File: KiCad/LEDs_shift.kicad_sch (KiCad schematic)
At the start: 37 parts, among them J101 2mm_clamp, J102 2mm_clamp, J103 2mm_clamp, J104 2mm_clamp, J105 2mm_clamp, J106 2mm_clamp, J107 2mm_clamp, J108 2mm_clamp, J109 2mm_clamp, J110 2mm_clamp, J111 2mm_clamp, J112 2mm_clamp, J113 2mm_clamp, J114 2mm_clamp, J115 2mm_clamp, J116 2mm_clamp, J117 2mm_clamp, J118 2mm_clamp, J119 2mm_clamp, J120 2mm_clamp, J121 2mm_clamp, J122 2mm_clamp, J123 2mm_clamp, J124 2mm_clamp, J125 2mm_clamp, J126 2mm_clamp, J127 2mm_clamp, J128 2mm_clamp, J129 2mm_clamp, U136 74HC595D,118, U137 74HC595D,118, U138 74HC595D,118, U139 74HC595D,118

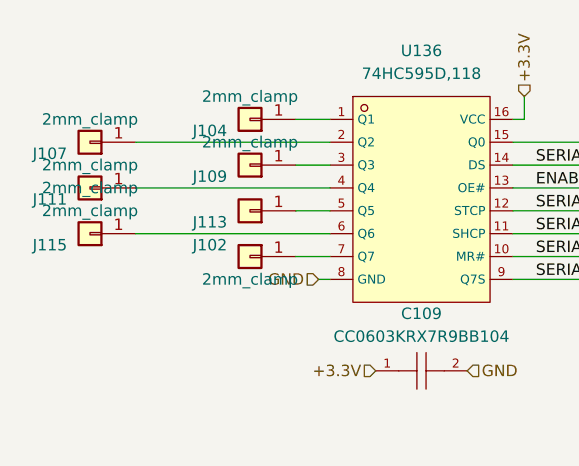
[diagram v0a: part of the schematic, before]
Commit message: Updated to not use adressable LED. Sch only
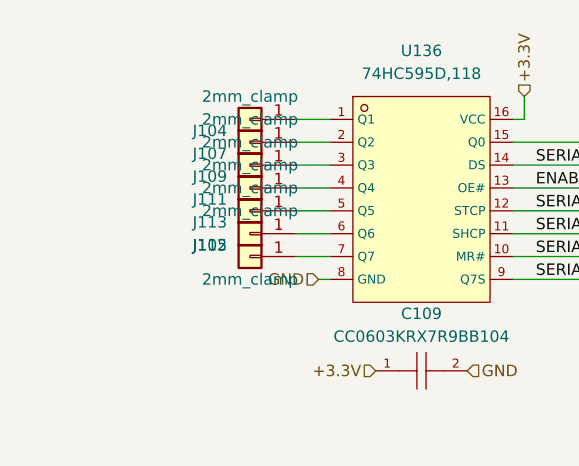
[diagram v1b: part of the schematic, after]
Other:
- moved on the sheet: J107, J111, J115
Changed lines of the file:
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@@
 (kicad_sch
-	(version 20250114)
+	(version 20231120)
 	(generator "eeschema")
-	(generator_version "9.0")
+	(generator_version "8.0")
 	(paper "A4")
 	(wire
@@
 	(wire
 		(pts
-			(xy 72.39 41.91) (xy 93.98 41.91)
+			(xy 90.17 41.91) (xy 93.98 41.91)
 		)
 		(stroke
@@
 	(wire
 		(pts
-			(xy 72.39 52.07) (xy 93.98 52.07)
+			(xy 90.17 52.07) (xy 93.98 52.07)
 		)
 		(stroke
@@
 	(wire
 		(pts
-			(xy 72.39 46.99) (xy 93.98 46.99)
+			(xy 90.17 46.99) (xy 93.98 46.99)
 		)
 		(stroke
@@
 	(label "SERIAL_CLOCK"
 		(at 203.2 49.53 0)
+		(fields_autoplaced yes)
 		(effects
 			(font
@@
 	(label "SERIAL_CLOCK"
 		(at 208.28 109.22 0)
+		(fields_autoplaced yes)
 		(effects
 			(font
@@
 	(label "SERIAL_CLOCK"
 		(at 116.84 52.07 0)
+		(fields_autoplaced yes)
 		(effects
 			(font
@@
 	(label "SERIAL_OUT_3"
 		(at 222.25 104.14 0)
+		(fields_autoplaced yes)
 		(effects
 			(font
@@
 	(label "SERIAL_OUT_3"
 		(at 123.19 116.84 0)
+		(fields_autoplaced yes)
 		(effects
 			(font
@@
 	(label "SERIAL_OUT_2"
 		(at 203.2 57.15 0)
+		(fields_autoplaced yes)
 		(effects
 			(font
@@
 	(label "SERIAL_RESET"
 		(at 123.19 114.3 0)
+		(fields_autoplaced yes)
 		(effects
 			(font
@@
 	(label "SERIAL_IN_1"
 		(at 116.84 44.45 0)
+		(fields_autoplaced yes)
 		(effects
 			(font
@@
 	(label "SERIAL_CLOCK"
 		(at 208.28 111.76 0)
+		(fields_autoplaced yes)
 		(effects
 			(font
@@
 	(label "ENABLE OUTPUT"
 		(at 116.84 46.99 0)
+		(fields_autoplaced yes)
 		(effects
 			(font
@@
 	(label "ENABLE OUTPUT"
 		(at 123.19 106.68 0)
+		(fields_autoplaced yes)
 		(effects
 			(font
@@
 	(label "SERIAL_OUT_2"
 		(at 137.16 104.14 0)
+		(fields_autoplaced yes)
 		(effects
 			(font
@@
 	(label "SERIAL_RESET"
 		(at 203.2 54.61 0)
+		(fields_autoplaced yes)
 		(effects
 			(font
@@
 	(label "SERIAL_CLOCK"
 		(at 116.84 49.53 0)
+		(fields_autoplaced yes)
 		(effects
 			(font
@@
 	(label "SERIAL_OUT_1"
 		(at 116.84 57.15 0)
+		(fields_autoplaced yes)
 		(effects
 			(font
@@
 	(label "SERIAL_CLOCK"
 		(at 203.2 52.07 0)
+		(fields_autoplaced yes)
 		(effects
 			(font
@@
 	(label "SERIAL_IN_4"
 		(at 208.28 104.14 0)
+		(fields_autoplaced yes)
 		(effects
 			(font
@@
 	(label "ENABLE OUTPUT"
 		(at 203.2 46.99 0)
+		(fields_autoplaced yes)
 		(effects
 			(font
@@
 	(label "SERIAL_RESET"
 		(at 208.28 114.3 0)
+		(fields_autoplaced yes)
 		(effects
 			(font
@@
 	(label "SERIAL_CLOCK"
 		(at 123.19 109.22 0)
+		(fields_autoplaced yes)
 		(effects
 			(font
@@
 	(label "SERIAL_IN_2"
 		(at 203.2 44.45 0)
+		(fields_autoplaced yes)
 		(effects
 			(font
@@
 	(label "SERIAL_CLOCK"
 		(at 123.19 111.76 0)
+		(fields_autoplaced yes)
 		(effects
 			(font
@@
 	(label "SERIAL_IN_3"
 		(at 123.19 104.14 0)
+		(fields_autoplaced yes)
 		(effects
 			(font
@@
 	(label "SERIAL_RESET"
 		(at 116.84 54.61 0)
+		(fields_autoplaced yes)
 		(effects
 			(font
@@
 	(label "ENABLE OUTPUT"
 		(at 208.28 106.68 0)
+		(fields_autoplaced yes)
 		(effects
 			(font
@@
 	(label "SERIAL_OUT_1"
 		(at 217.17 44.45 0)
+		(fields_autoplaced yes)
 		(effects
 			(font
@@
 		(shape input)
 		(at 134.62 54.61 0)
+		(fields_autoplaced yes)
 		(effects
 			(font
@@
 		(shape input)
 		(at 201.93 36.83 90)
+		(fields_autoplaced yes)
 		(effects
 			(font
@@
 		(shape input)
 		(at 105.41 127 180)
+		(fields_autoplaced yes)
 		(effects
 			(font
@@
 		(shape input)
 		(at 99.06 67.31 180)
+		(fields_autoplaced yes)
 		(effects
 			(font
@@
 		(shape input)
 		(at 186.69 68.58 180)
+		(fields_autoplaced yes)
 		(effects
 			(font
@@
 		(shape input)
 		(at 134.62 46.99 0)
+		(fields_autoplaced yes)
 		(effects
 			(font
@@
 		(shape input)
 		(at 134.62 49.53 0)
+		(fields_autoplaced yes)
 		(effects
 			(font
@@
 		(shape input)
 		(at 115.57 36.83 90)
+		(fields_autoplaced yes)
 		(effects
 			(font
@@
 		(shape input)
 		(at 115.57 127 0)
+		(fields_autoplaced yes)
 		(effects
 			(font
@@
 		(shape input)
 		(at 184.15 116.84 180)
+		(fields_autoplaced yes)
 		(effects
 			(font
@@
 		(shape input)
 		(at 190.5 127 180)
+		(fields_autoplaced yes)
 		(effects
 			(font
@@
 		(shape input)
 		(at 121.92 96.52 90)
+		(fields_autoplaced yes)
 		(effects
 			(font
@@
 		(shape input)
 		(at 196.85 68.58 0)
+		(fields_autoplaced yes)
 		(effects
 			(font
@@
 		(shape input)
 		(at 207.01 96.52 90)
+		(fields_autoplaced yes)
 		(effects
 			(font
@@
 		(shape input)
 		(at 179.07 57.15 180)
+		(fields_autoplaced yes)
 		(effects
 			(font
@@
 		(shape input)
 		(at 99.06 116.84 180)
+		(fields_autoplaced yes)
 		(effects
 			(font
@@
 		(shape input)
 		(at 200.66 127 0)
+		(fields_autoplaced yes)
 		(effects
 			(font
@@
 		(shape input)
 		(at 92.71 57.15 180)
+		(fields_autoplaced yes)
 		(effects
 			(font
@@
 		(shape input)
 		(at 134.62 44.45 0)
+		(fields_autoplaced yes)
 		(effects
 			(font
@@
 		(shape input)
 		(at 109.22 67.31 0)
+		(fields_autoplaced yes)
 		(effects
 			(font
@@
 		(shape input)
 		(at 134.62 52.07 0)
+		(fields_autoplaced yes)
 		(effects
 			(font
@@
 		(on_board yes)
 		(dnp no)
+		(fields_autoplaced yes)
 		(property "Reference" "J113"
 			(at 82.55 50.8 0)
@@
 		)
 		(property "Value" "2mm_clamp"
-			(at 67.31 46.99 0)
+			(at 85.09 46.99 0)
 			(effects
 				(font
@@
 	(symbol
 		(lib_id "Kaboom_box:2mm_clamp")
-		(at 67.31 52.07 180)
+		(at 85.09 52.07 180)
 		(unit 1)
 		(exclude_from_sim no)
@@
 		(fields_autoplaced yes)
 		(property "Reference" "J115"
-			(at 64.77 53.34 0)
+			(at 82.55 53.34 0)
 			(effects
 				(font
@@
 		)
 		(property "Value" "2mm_clamp"
-			(at 67.31 49.53 0)
+			(at 85.09 49.53 0)
 			(effects
 				(font
@@
 		)
 		(property "Footprint" "Kaboom_box:2mm testlead, screw-clamp"
-			(at 68.58 46.99 0)
+			(at 86.36 46.99 0)
 			(effects
 				(font
@@
 		)
 		(property "Datasheet" "https://www.aliexpress.com/item/1005003745780405.html?spm=a2g0o.order_list.order_list_main.12.1f5c18020OVUCx"
-			(at 69.85 44.45 0)
+			(at 87.63 44.45 0)
 			(effects
 				(font
@@
 		)
 		(property "Description" ""
-			(at 67.31 52.07 0)
+			(at 85.09 52.07 0)
 			(effects
 				(font
@@
 	(symbol
 		(lib_id "Kaboom_box:2mm_clamp")
-		(at 67.31 41.91 180)
+		(at 85.09 41.91 180)
 		(unit 1)
 		(exclude_from_sim no)
@@
 		(fields_autoplaced yes)
 		(property "Reference" "J107"
-			(at 64.77 43.18 0)
+			(at 82.55 43.18 0)
 			(effects
 				(font
@@
 		)
 		(property "Value" "2mm_clamp"
-			(at 67.31 39.37 0)
+			(at 85.09 39.37 0)
 			(effects
 				(font
@@
 		)
 		(property "Footprint" "Kaboom_box:2mm testlead, screw-clamp"
-			(at 68.58 36.83 0)
+			(at 86.36 36.83 0)
 			(effects
 				(font
@@
 		)
 		(property "Datasheet" "https://www.aliexpress.com/item/1005003745780405.html?spm=a2g0o.order_list.order_list_main.12.1f5c18020OVUCx"
-			(at 69.85 34.29 0)
+			(at 87.63 34.29 0)
 			(effects
 				(font
@@
 		)
 		(property "Description" ""
-			(at 67.31 41.91 0)
+			(at 85.09 41.91 0)
 			(effects
 				(font
@@
 	(symbol
 		(lib_id "Kaboom_box:2mm_clamp")
-		(at 67.31 46.99 180)
+		(at 85.09 46.99 180)
 		(unit 1)
 		(exclude_from_sim no)
@@
 		(on_board yes)
 		(dnp no)
+		(fields_autoplaced yes)
 		(property "Reference" "J111"
-			(at 64.77 48.26 0)
+			(at 82.55 48.26 0)
 			(effects
 				(font
@@
 		)
 		(property "Value" "2mm_clamp"
-			(at 67.31 44.45 0)
+			(at 85.09 44.45 0)
 			(effects
 				(font
@@
 		)
 		(property "Footprint" "Kaboom_box:2mm testlead, screw-clamp"
-			(at 68.58 41.91 0)
+			(at 86.36 41.91 0)
 			(effects
 				(font
@@
 		)
 		(property "Datasheet" "https://www.aliexpress.com/item/1005003745780405.html?spm=a2g0o.order_list.order_list_main.12.1f5c18020OVUCx"
-			(at 69.85 39.37 0)
+			(at 87.63 39.37 0)
 			(effects
 				(font
@@
 		)
 		(property "Description" ""
-			(at 67.31 46.99 0)
+			(at 85.09 46.99 0)
 			(effects
 				(font
